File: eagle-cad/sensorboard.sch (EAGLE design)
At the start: 37 parts, among them IC1 MCP1702-33, U1 ATMEGA328P_PDIP, Y1 16MHz

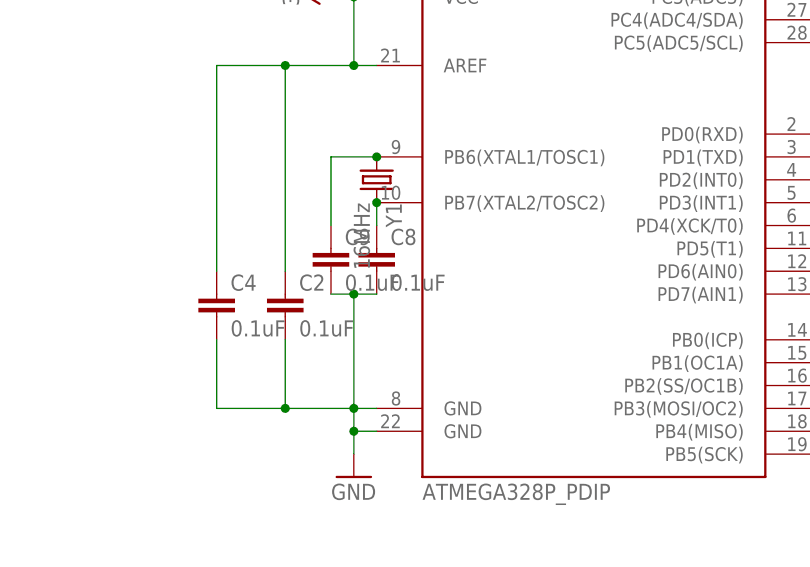
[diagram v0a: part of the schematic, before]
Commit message: Fixed crystal cap values
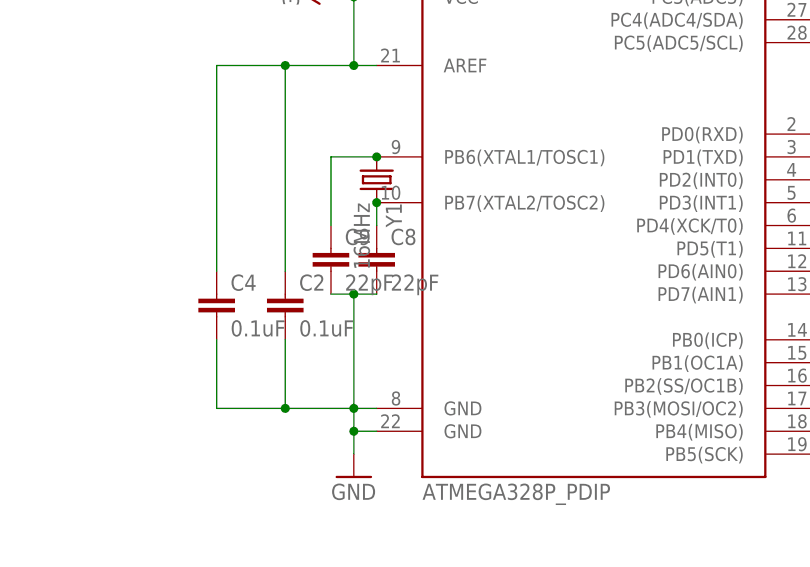
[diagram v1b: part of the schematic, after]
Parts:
- C8, C9: value 0.1uF -> 22pF
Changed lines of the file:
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@@
 <?xml version="1.0" encoding="utf-8"?>
 <!DOCTYPE eagle SYSTEM "eagle.dtd">
-<eagle version="6.4">
+<eagle version="6.5.0">
 <drawing>
 <settings>
@@
 <part name="GND22" library="supply1" deviceset="GND" device=""/>
 <part name="P+23" library="SparkFun-Aesthetics" deviceset="3.3V" device=""/>
-<part name="C8" library="SparkFun-Capacitors" deviceset="CAP" device="EZ" value="0.1uF"/>
-<part name="C9" library="SparkFun-Capacitors" deviceset="CAP" device="EZ" value="0.1uF"/>
+<part name="C8" library="SparkFun-Capacitors" deviceset="CAP" device="EZ" value="22pF"/>
+<part name="C9" library="SparkFun-Capacitors" deviceset="CAP" device="EZ" value="22pF"/>
 <part name="Y1" library="SparkFun-FreqCtrl" deviceset="CRYSTAL" device="HC49US" value="16MHz"/>
 <part name="VCC+" library="SparkFun-Connectors" deviceset="M01" device="PTH_2MM"/>

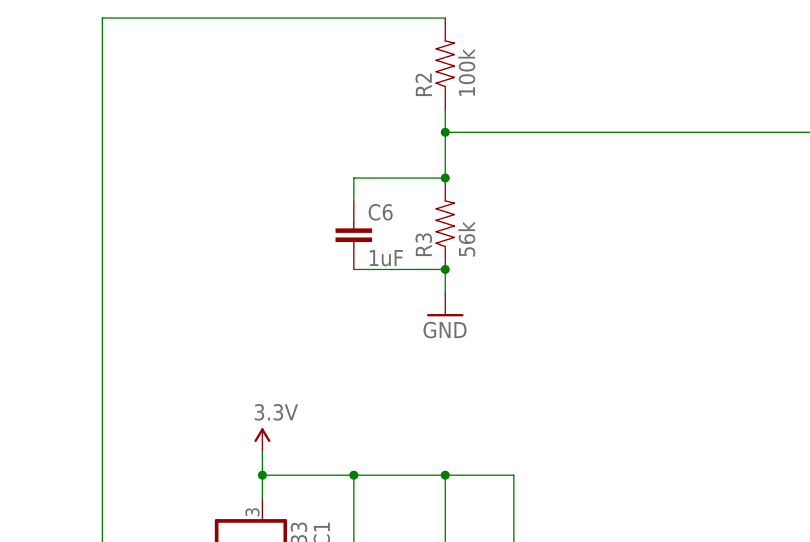
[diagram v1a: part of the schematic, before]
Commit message: Fixed resistor divider cap value
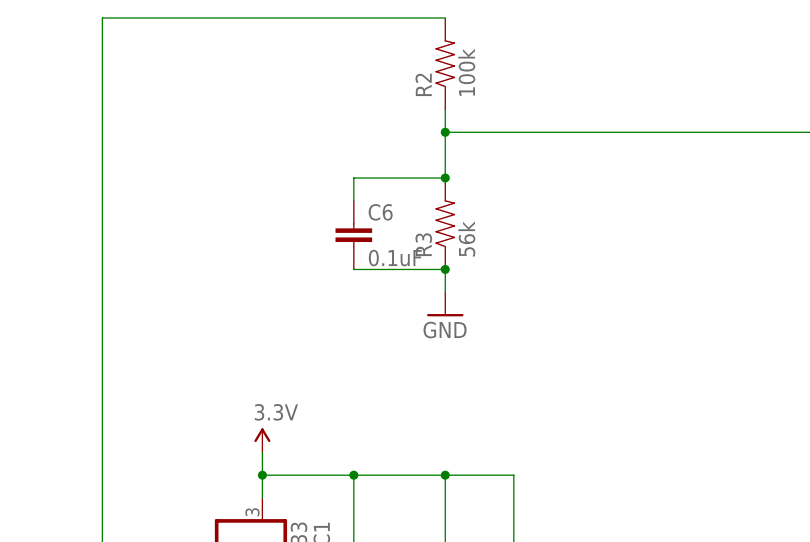
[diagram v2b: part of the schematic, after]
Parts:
- C6: value 1uF -> 0.1uF
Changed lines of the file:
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@@
 <part name="R3" library="SparkFun-Resistors" deviceset="RESISTOR" device="EZ" value="56k"/>
 <part name="GND5" library="supply1" deviceset="GND" device=""/>
-<part name="C6" library="SparkFun-Capacitors" deviceset="CAP" device="EZ" value="1uF"/>
+<part name="C6" library="SparkFun-Capacitors" deviceset="CAP" device="EZ" value="0.1uF"/>
 <part name="GND7" library="supply1" deviceset="GND" device=""/>
 <part name="25" library="SparkFun-Connectors" deviceset="M03" device="1X03_NO_SILK"/>
